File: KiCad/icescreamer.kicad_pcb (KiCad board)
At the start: 2 copper layers, 60 x 85 mm, 93 parts, among them J1 Audio-Jack-3_3Switches, J2 Audio-Jack-3_3Switches, J3 Barrel_Jack_Switch, Q1 BC547, Q2 BC547, Q20 BC547, Q21 BC547, Q22 BC547, Q23 Q_NJFET_SGD, Q24 Q_NJFET_SGD, SW1 SW_TruBy, SW20 SW_Push, U1 NE5532

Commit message: mandado a fabricar, ya no hay vuelta atrás
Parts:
- removed the G*** at (213.4, 110.9)
- removed the G*** at (213.8, 110.7)
- added G***: LOGO, IceScreamer:PickLogoThinSilk_15mm, B.Cu at (197.1, 80.3)
- added G***: LOGO, IceScreamer:IceLogoMask, B.Cu at (229.6, 73.5)
- added G***: LOGO, IceScreamer:IceLogoSilk, B.Cu at (229.5, 75.1)
- added G***: LOGO, prueba:Font0, B.Cu at (213.6, 104.7)
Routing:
- net Net-(D21-Pad2): track 66.7 -> 62.6 mm, vias 2 -> 3
- net Net-(D20-Pad2): track 58.8 -> 58.2 mm
- net PSEUDO_OUT: track 71.3 -> 70.7 mm, vias 1 -> 0
- net +VDC: track 211.5 -> 212.0 mm
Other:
- board text added: "Board & upgrades: JorFru V0.3"
- board text removed: "Board & upgrades: JorFru"

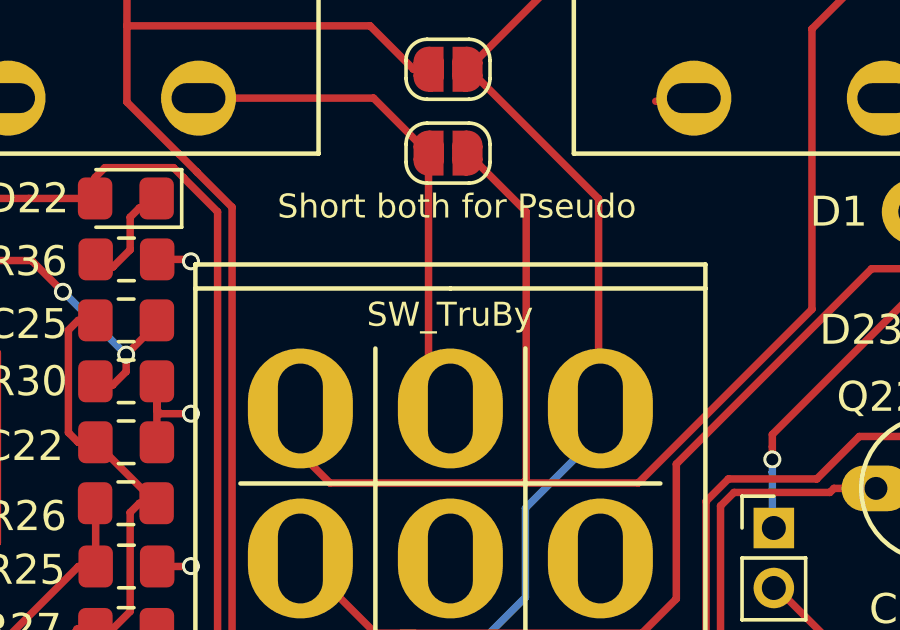
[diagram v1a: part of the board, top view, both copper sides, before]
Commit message: update de la PCB con los valores de los componentes marcados
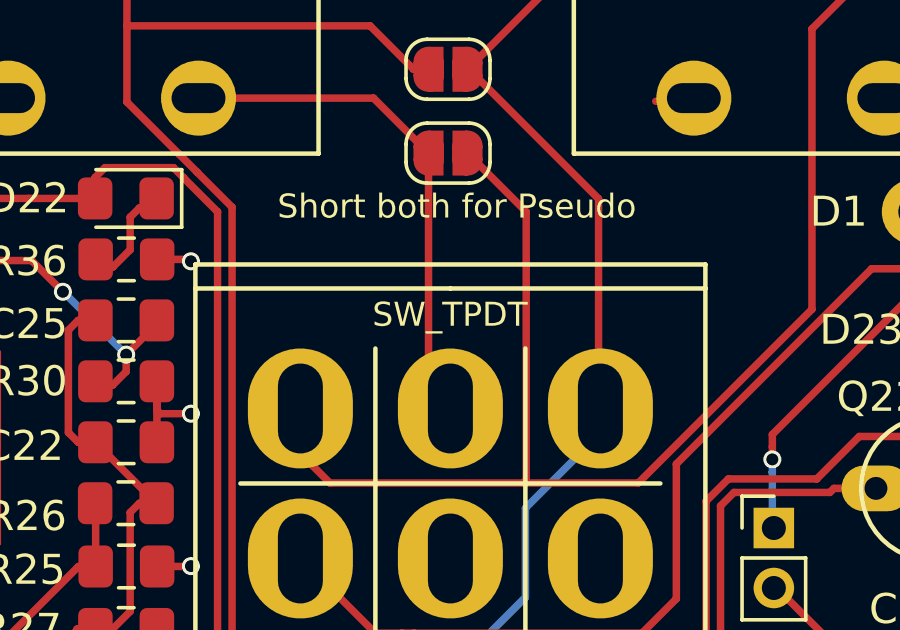
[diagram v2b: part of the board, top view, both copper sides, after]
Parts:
- C1, C2: value CP -> 220uF
- C10, C9: value C -> 220nF
- C11, C6: value C -> 1uF
- C12, C14, C15, C16, C17, C18, C20, C3, C4: value C -> 100nF
- C13: value C -> 10uF
- C21, C27: value C -> 47nF
- C22, C25, C26: value C -> 1nF
- C23, C24: value C -> 100pF
- C5: value C -> 22nF
- C7, C8: value C -> 47pF
- D1: value D -> 1N4001
- D2, D20, D21, D22, D3: value D -> 1N4148
- D23: value D_Zener -> 4V7_Zener
- J1, J2: value Audio-Jack-3_3Switches -> NMJ6HFD2
- POT1: value POT -> log 470k
- POT2: value POT -> lin 22K
- POT3: value POT -> log 100K
- Q1, Q2, Q20, Q21, Q22: value BC547 -> NPN_BC547
- Q23, Q24: value Q_NJFET_SGD -> MMBF4392L
- R1, R10, R15, R17, R19, R2, R5, R6: value R -> 10K
- R11, R13, R3, R9: value R -> 1K
- R12: value R -> 220R
- R14, R20, R21, R4: value R -> 470K
- R16, R36: value R -> 100R
- R22, R26, R32: value R -> 1M
- R23, R24, R30, R31, R34: value R -> 56K
- R25: value R -> 22K
- R27: value R -> 22R
- R28, R29, R7: value R -> 47K
- R33: value R -> 0R
- R35: value R -> 36K
- R8: value R -> 4K7
- SW1: value SW_TruBy -> SW_TPDT
- U1: value NE5532 -> RC4558
